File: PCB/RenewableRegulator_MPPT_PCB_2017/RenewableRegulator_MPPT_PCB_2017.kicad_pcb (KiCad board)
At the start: 2 copper layers, 99.6 x 90.8 mm, 62 parts, among them J1 TEMP, J2 Arduino_Nano, P1 INPUT, P10 TP_FET, P11 TP_GND, P12 TP_5V, P13 TP_10V, P2 Vref?, P3 MicroSD, P4 A6_7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

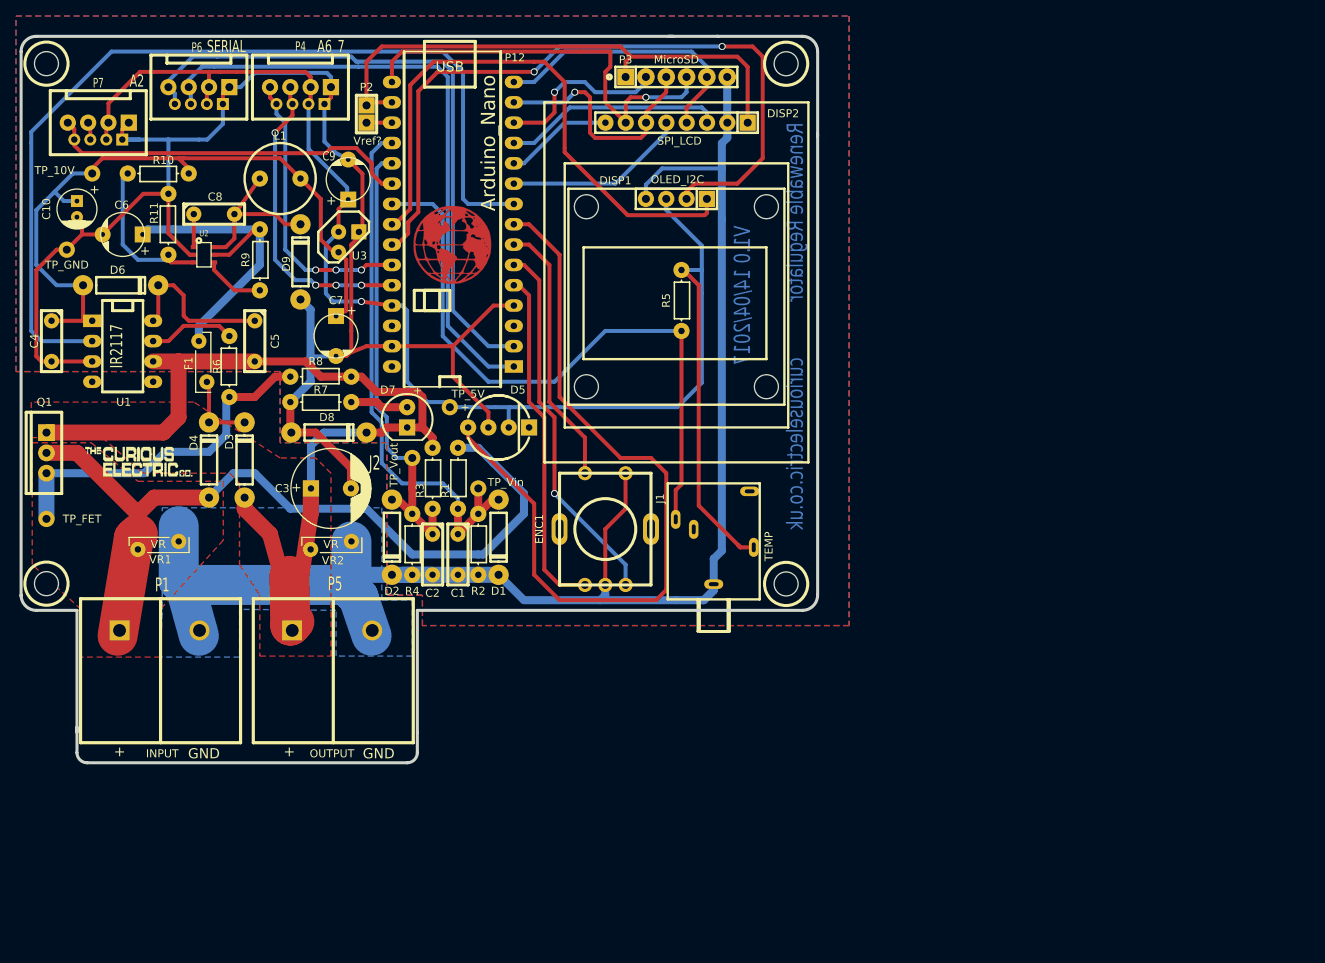
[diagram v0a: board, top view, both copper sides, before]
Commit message: First version MPPT PCB
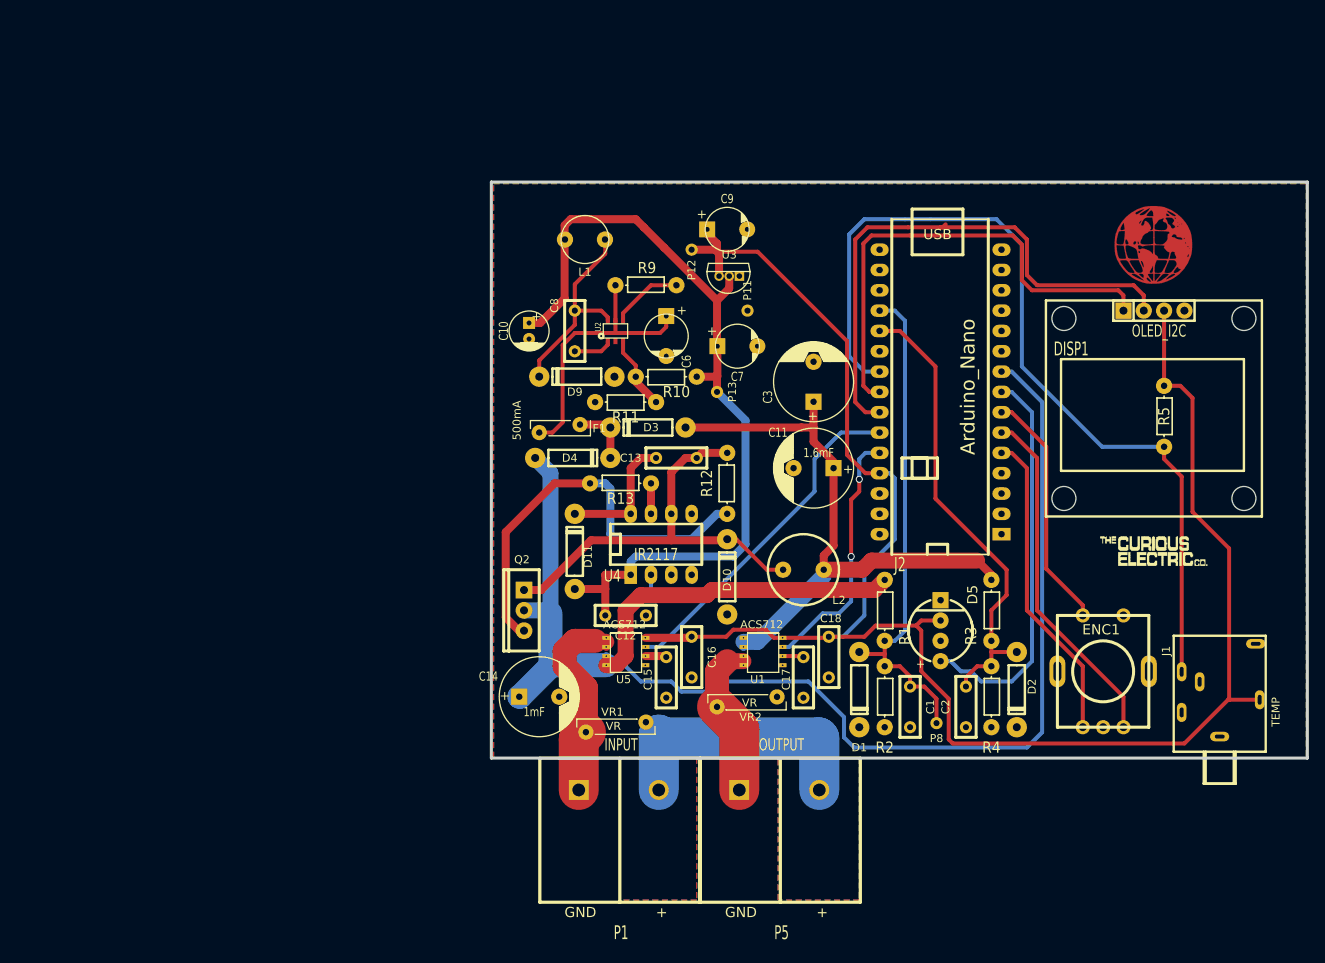
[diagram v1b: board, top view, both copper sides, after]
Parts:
- removed C4, C5: 100nf, matts_components:C1_wide_lg_pad
- removed D6: 1N5822, REInnovationFootprint:TH_Diode_1
- removed D7: LED, REInnovationFootprint:TH_LED-5MM_larg_pad
- removed D8: UF4002, REInnovationFootprint:TH_Diode_1
- removed DISP2: SPI_LCD, REInnovationFootprint:TH_LCD_SPI_128x128
- removed MH1: Mounting holes, RenewableRegulatorPCB_2017_Library_Yoan:3mm_hole
- removed MH1 (x3): CONN_1, RenewableRegulatorPCB_2017_Library_Yoan:3mm_hole
- removed P10: TP_FET, matts_components:1pin_0_8mm
- removed P2: Vref?, matts_components:SIL-2_solder_connect
- removed P3: MicroSD, matts_components:SIL-6_large_pads_marker
- removed P4: A6_7, matts_components:SIL-4_Grove_SIL
- removed P6: SERIAL, matts_components:SIL-4_Grove_SIL
- removed P7: A2, matts_components:SIL-4_Grove_SIL
- removed P9: TP_Vout, matts_components:1pin_0_8mm
- removed Q1: TK32A12N1, matts_components:TO220_VERT_BUZ11_matt
- removed R6: 5, REInnovationFootprint:TH_Resistor_1
- removed R7: 1k, REInnovationFootprint:TH_Resistor_1
- removed R8: 100k, REInnovationFootprint:TH_Resistor_1
- added C11: 1.6mF, RenewableRegulatorPCB_2017_Library_Yoan:Capacitor_C_1V7_TH, F.Cu at (161.9, 99.7)
- added C12: 100nf, REInnovationFootprint:cond_1, F.Cu at (134.6, 119.4)
- added C13: 100nf, REInnovationFootprint:cond_1, F.Cu at (141.0, 99.7)
- added C14: 1mF, RenewableRegulatorPCB_2017_Library_Yoan:Capacitor_C_1V7_TH, F.Cu at (127.6, 128.3)
- added C15: 1nf, REInnovationFootprint:cond_1, F.Cu at (142.2, 122.0)
- added C16: 0.1µF, REInnovationFootprint:cond_1, F.Cu at (145.4, 119.5)
- added C17: 1nf, REInnovationFootprint:cond_1, F.Cu at (159.4, 122.0)
- added C18: 0.1µF, REInnovationFootprint:cond_1, F.Cu at (162.6, 119.5)
- added D10: DIODE, REInnovationFootprint:TH_Diode_1, F.Cu at (151.1, 113.7)
- added D11: 1N5822, REInnovationFootprint:TH_Diode_1, F.Cu at (132.1, 110.5)
- added L2: 100µH, REInnovationFootprint:TH_Inductor, F.Cu at (160.7, 112.4)
- added Q2: TK32A12N1, REInnovationFootprint:TO220_VERT_BUZ11_matt, F.Cu at (125.7, 117.5)
- added R12: 100k, REInnovationFootprint:TH_Resistor_1, F.Cu at (151.1, 101.6)
- added R13: 5, REInnovationFootprint:TH_Resistor_1, F.Cu at (137.8, 101.6)
- added U4: IR2117, REInnovationFootprint:DIP-8_300_ELL, F.Cu at (146.7, 109.2)
- added U5: ACS712, acs712:acs712, F.Cu at (136.5, 125.2)
- C1, C2, C8: footprint matts_components:C1_wide_lg_pad -> REInnovationFootprint:cond_1
- DISP1: footprint TH_OLED1306 -> REInnovationFootprint:TH_OLED1306
- L1: footprint REInnovationFootprint:TH_Inductor -> REInnovationFootprint:TH_Inductor2
- P11, P12, P13, P8: footprint matts_components:1pin_0_8mm -> REInnovationFootprint:tp
- U1: value IR2117 -> ACS712; footprint REInnovationFootprint:DIP-8_300_ELL -> acs712:acs712
- U3: footprint matts_components:TO92_MCP9701_matt -> REInnovationFootprint:TO92_MCP9701_matt2
- moved LOGO2 127.4 mm to (197.5, 108.0)
- moved LOGO1 87.6 mm to (204.5, 71.8)
- moved U1 86.1 mm to (153.7, 125.2), turned to 0 degrees
- moved P11 85.4 mm to (153.7, 80.0), turned to 90 degrees
- moved P13 82.7 mm to (149.9, 90.2), turned to 90 degrees
- moved D2 80.4 mm to (187.3, 127.0)
- moved R4 74.9 mm to (184.2, 128.3)
- moved R3 71.8 mm to (184.2, 117.5)
- moved C6 69.1 mm to (143.5, 83.2), turned to 270 degrees
- moved R10 68.4 mm to (143.5, 88.3)
- moved C2 67.5 mm to (179.7, 125.7)
- moved VR1 67.1 mm to (141.0, 131.4), turned to 180 degrees
- moved J1 66.1 mm to (218.4, 120.7)
- moved ENC1 64.7 mm to (198.1, 125.1)
- moved J2 64.5 mm to (177.8, 83.8)
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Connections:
- D5 pad 1: (no net) -> Net-(D5-Pad1)
- J1 pad 5: (no net) -> Net-(J1-Pad5)
- J1 pad 6: (no net) -> Net-(J1-Pad6)
- J2 pad 10: LCD_DC -> Net-(J2-Pad10)
- J2 pad 11: LCD_BL -> Net-(J2-Pad11)
- J2 pad 12: LCD_CS -> Net-(J2-Pad12)
- J2 pad 25: A6 -> VcurrentInput
- J2 pad 26: A7 -> VcurrentOutput
- J2 pad 28: (no net) -> Net-(J2-Pad28)
- J2 pad 3: (no net) -> Net-(J2-Pad3)
- J2 pad 30: (no net) -> Net-(J2-Pad30)
- LOGO1 pad 1: (no net) -> Net-(LOGO1-Pad1)
- P1 pad 1: Vinput -> /currentMeasurmentin/IN
- P5 pad 1: Voutput -> /currentMeasurmentout/OUT
- U1 pad 1: /Power Supply/+10V -> Voutput
- U1 pad 2: FET1 -> Voutput
- U1 pad 3: GND -> /currentMeasurmentout/OUT
- U1 pad 4: (no net) -> /currentMeasurmentout/OUT
- U1 pad 5: (no net) -> GND
- U1 pad 6: Voutput -> Net-(C17-Pad1)
- U1 pad 7: Net-(R6-Pad2) -> VcurrentOutput
- U1 pad 8: Net-(C5-Pad1) -> +5V
- VR1 pad 1: Vinput -> GND
- VR1 pad 2: GND -> /currentMeasurmentin/IN
- VR2 pad 1: Voutput -> /currentMeasurmentout/OUT
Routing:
- net GND: track 402.6 -> 33.6 mm
- net Rx: track 80.1 -> 0.00 mm
- net Tx: track 78.2 -> 0.00 mm
- net +3V3: track 68.7 -> 0.00 mm
- net Voutput: track 139.1 -> 76.7 mm
- net Net-(C13-Pad2): track 0.00 -> 53.1 mm
- net SCK: track 53.2 -> 0.36 mm, vias 1 -> 0
- net Net-(Q2-PadG): track 0.00 -> 51.4 mm
- net LED_D: track 97.1 -> 49.5 mm
- net A2: track 46.1 -> 0.00 mm
- net Net-(P10-Pad1): track 43.7 -> 0.00 mm
- net VcurrentInput: track 0.00 -> 42.8 mm
- net A7: track 38.5 -> 0.00 mm, vias 4 -> 0
- net A6: track 35.8 -> 0.00 mm, vias 3 -> 0
- net MISO: track 34.5 -> 0.00 mm
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- removed copper zone on F.Cu, net Vinput
- removed copper zone on F.Cu, net Voutput
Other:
- board size 99.6 x 90.8 mm -> 102 x 72 mm
- net class Default: trace_width 1 -> 0.5
- board text removed: "Renewable Regulator"
- board text removed: "V1.0 14/04/2017"
- board text removed: "curiouselectric.co.uk"

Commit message: Updated PCB of MPPT
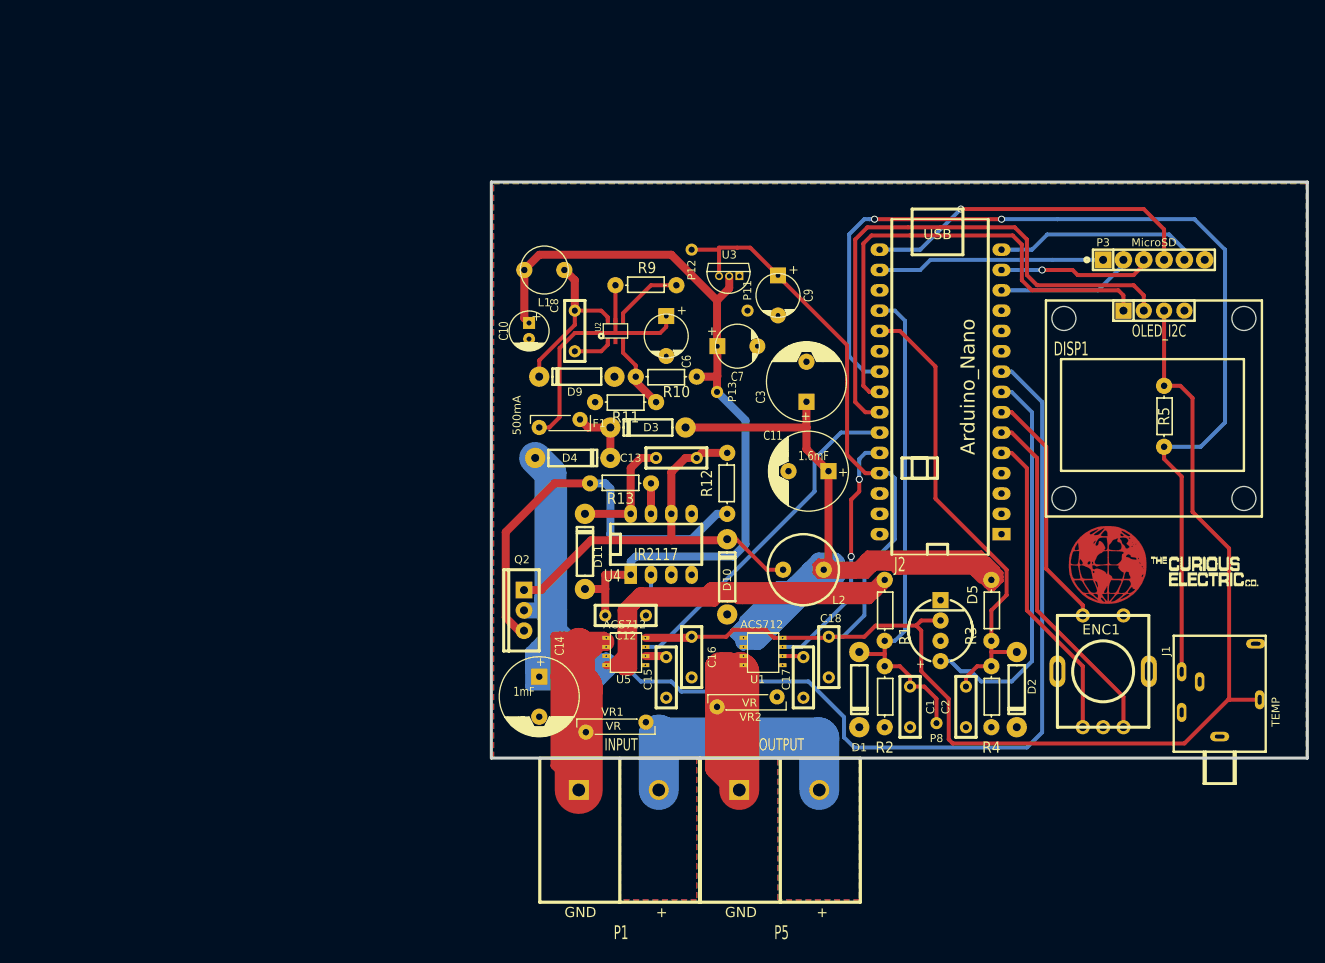
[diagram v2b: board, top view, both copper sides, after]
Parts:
- added P3: MicroSD, REInnovationFootprint:SIL-6_large_pads_marker, F.Cu at (204.5, 73.7)
- moved LOGO1 40.4 mm to (198.8, 111.8)
- moved C9 10.4 mm to (157.5, 78.1), turned to 270 degrees
- moved LOGO2 6.84 mm to (203.8, 110.5)
- moved L1 6.35 mm to (128.3, 74.9)
- moved D11 1.27 mm to (133.3, 110.5)
- moved C3 0.89 mm to (161.0, 88.9)
- moved C11 0.74 mm to (161.3, 100.1)
- moved F1 0.64 mm to (127.6, 94.6)
- turned C14 to 270 degrees
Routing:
- net Voutput: track 76.7 -> 277.7 mm
- net Vinput: track 86.4 -> 232.6 mm
- net /currentMeasurmentin/IN: track 25.8 -> 105.1 mm
- net SCK: track 0.36 -> 42.9 mm, vias 0 -> 1
- net +3V3: track 0.00 -> 28.5 mm
- net MISO: track 0.00 -> 25.7 mm
- net /currentMeasurmentout/OUT: track 21.0 -> 41.6 mm
- net MOSI: track 0.00 -> 19.2 mm, vias 0 -> 1
- net TEMP: track 109.7 -> 128.7 mm, vias 0 -> 2
- net SD_CS: track 0.00 -> 17.2 mm
- net /Power Supply/+10V: track 105.7 -> 100.1 mm
- net Net-(C8-Pad2): track 25.5 -> 20.7 mm
- net +5V: track 225.3 -> 222.3 mm
- net Net-(C13-Pad1): track 16.4 -> 15.1 mm
- net /Power Supply/+PWR: track 34.3 -> 33.5 mm
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
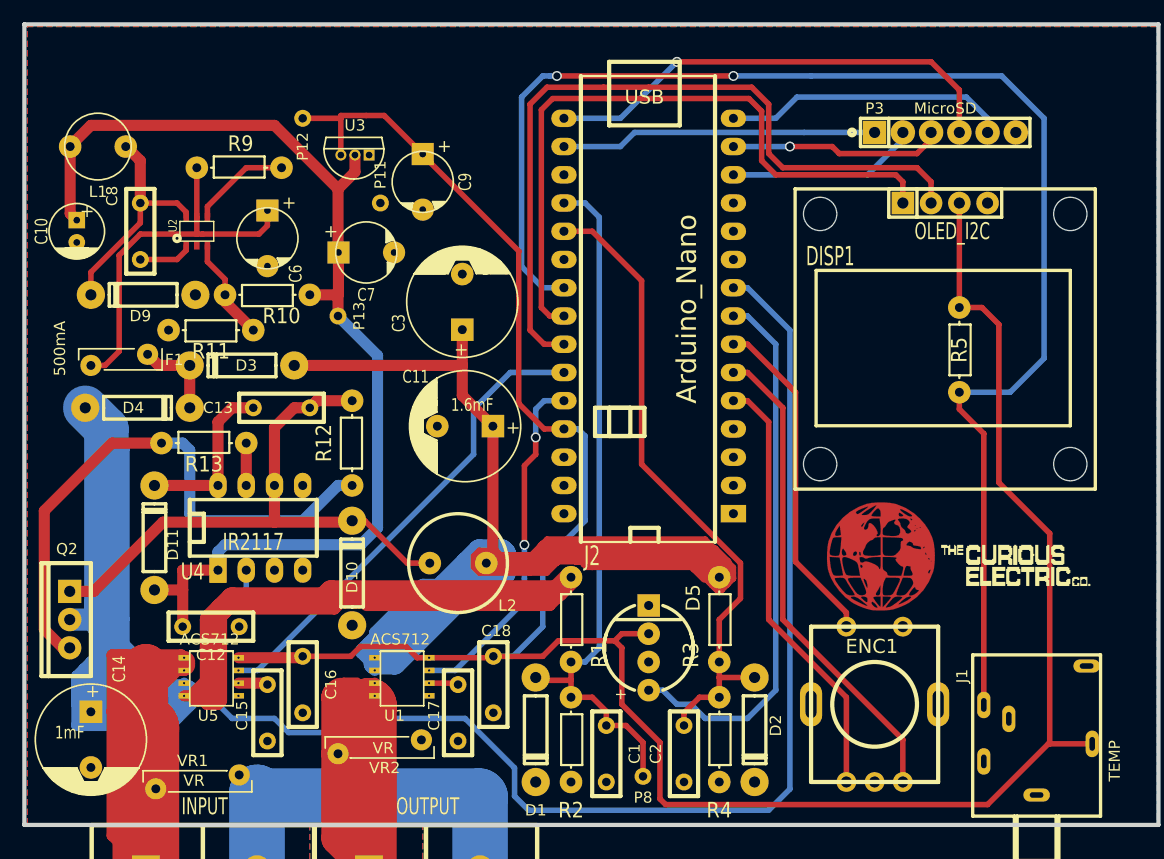
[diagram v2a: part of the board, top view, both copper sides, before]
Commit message: Updated MPPT PCB
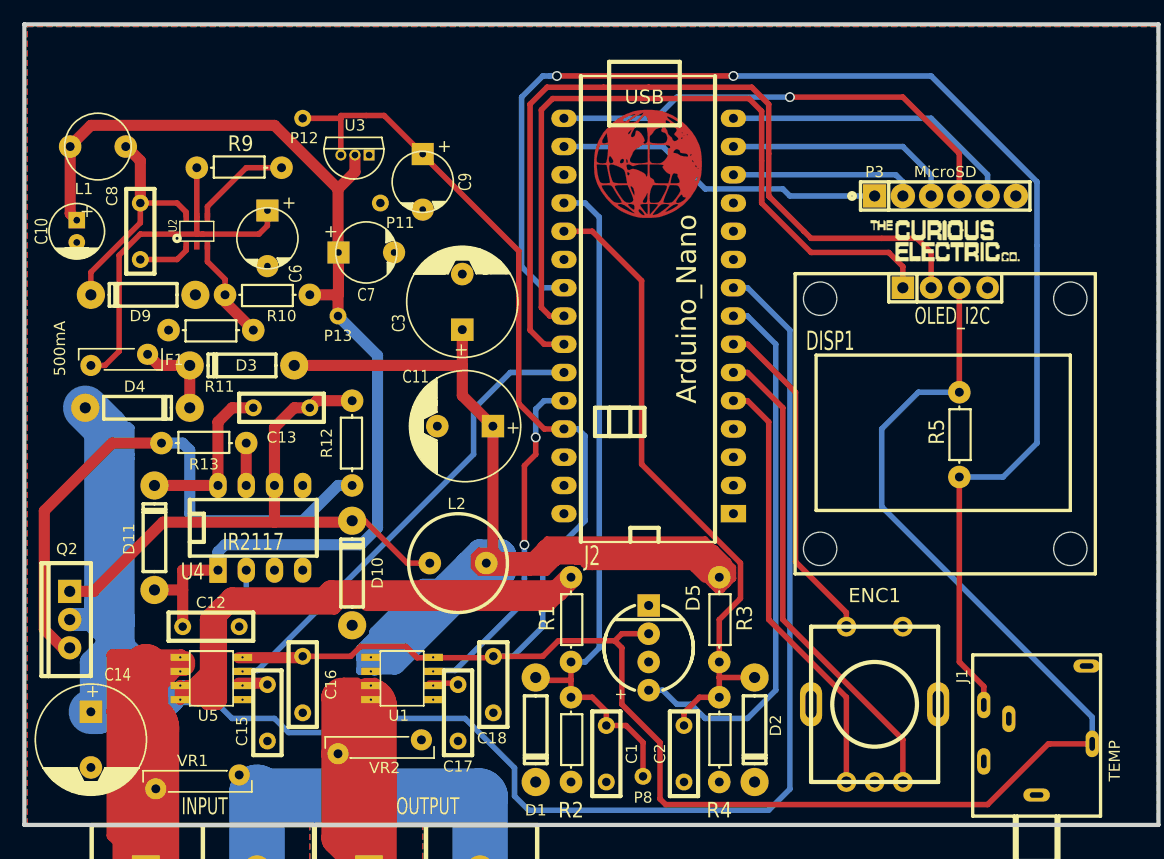
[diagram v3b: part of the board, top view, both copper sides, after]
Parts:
- moved LOGO1 41.1 mm to (177.8, 76.5)
- moved LOGO2 29.9 mm to (197.5, 81.3)
- moved DISP1 7.62 mm to (204.5, 86.4)
- moved R5 7.62 mm to (205.7, 100.8)
- moved P3 5.72 mm to (204.5, 79.4)
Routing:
- net Vinput: track 232.6 -> 269.9 mm
- net Voutput: track 277.7 -> 285.5 mm
- net SCL: track 68.6 -> 74.9 mm
- net SDA: track 60.7 -> 66.1 mm
- net TEMP: track 128.7 -> 124.1 mm
- net MOSI: track 19.2 -> 20.7 mm, vias 1 -> 0
- net +3V3: track 28.5 -> 29.8 mm
- net MISO: track 25.7 -> 26.9 mm
- net +5V: track 222.3 -> 223.1 mm
